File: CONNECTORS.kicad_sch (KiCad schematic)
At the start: 0 parts

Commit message: added micro and 3 sensors and connectors with USB
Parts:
- added D1: B5819W, Diode_SMD:D_SOD-123, symbol Device:D_Schottky
- added J1: STDC14, Connector_PinHeader_1.27mm:PinHeader_2x07_P1.27mm_Vertical_SMD, symbol Connector:Conn_ST_STDC14
- added J2: Screw_Terminal_01x02, symbol Connector:Screw_Terminal_01x02
- added J3: ARM_SW, Connector_JST:JST_GH_SM02B-GHS-TB_1x02-1MP_P1.25mm_Horizontal, symbol Connector_Generic:Conn_01x02
- added J4: CAMERA, Connector_JST:JST_GH_SM04B-GHS-TB_1x04-1MP_P1.25mm_Horizontal, symbol Connector_Generic:Conn_01x04
- added J5: USB_C, Connector_USB:USB_C_Receptacle_HRO_TYPE-C-31-M-12, symbol Connector:USB_C_Receptacle_USB2.0_16P
- added Q1: AO3401A, Package_TO_SOT_SMD:SOT-23, symbol Transistor_FET:AO3401A
- added R10, R11: 5.1k 1%, Resistor_SMD:R_0603_1608Metric, symbol Device:R
- added R4: 10KΩ 1% 0603, symbol Device:R
- added TP1: BATT_TERM+, symbol Connector:TestPoint
- added TP2: GND, symbol Connector:TestPoint
- added TP3: POST_PFET, symbol Connector:TestPoint
- added U7: USBLC6-2SC6, Package_TO_SOT_SMD:SOT-23-6, symbol Power_Protection:USBLC6-2SC6
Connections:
- new net: D1.2 (A), J5.A4 (VBUS), J5.A9 (VBUS), J5.B4 (VBUS), J5.B9 (VBUS), U7.5 (VBUS)
- new net: J5.A5 (CC1), R10.1
- new net: J5.B5 (CC2), R11.1
- new net: Q1.1 (G), R4.1
- new net +BATT: Q1.2 (S), TP3.1
- new net 3V3: J1.3 (VCC)
- new net 5V0: D1.1 (K), J4.1 (Pin_1)
- new net BATT_RAW: J2.1 (Pin_1), J3.1 (Pin_1), TP1.1
- new net BATT_SW: J3.2 (Pin_2), Q1.3 (D)
- new net CAM_RX: J4.3 (Pin_3)
- new net CAM_TX: J4.2 (Pin_2)
- new net DBG_RX: J1.13 (VCP_RX)
- new net DBG_TX: J1.14 (VCP_TX)
- new net GND: J1.11 (GNDDetect), J1.5 (GND), J1.7 (GND), J2.2 (Pin_2), J4.4 (Pin_4), J5.A1 (GND), J5.A12 (GND), J5.B1 (GND), J5.B12 (GND), J5.SH (SHIELD), R10.2, R11.2, R4.2, TP2.1, U7.2 (GND)
- new net NRST: J1.12 (~{RST})
- new net SWCLK: J1.6 (JCLK/SWCLK)
- new net SWDIO: J1.4 (JTMS/SWDIO)
- new net SWO: J1.8 (JTDO/SWO)
- new net USB_DM: J5.A7 (D-), J5.B7 (D-), U7.3 (I/O2), U7.4 (I/O2)
- new net USB_DP: J5.A6 (D+), J5.B6 (D+), U7.1 (I/O1), U7.6 (I/O1)
- no-connect marks 0 -> 4
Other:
- note added: "BATT_SW"
- note added: "CAM"
- note added: "DEBUGGER"
- note added: "Reverse Polarity"
- note added: "USB-C"

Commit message: added Buzzer, status LEDs
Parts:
- J2: value Screw_Terminal_01x02 -> XT30PW-M; footprint (none) -> Connector_AMASS:AMASS_XT30PW-M_1x02_P2.50mm_Horizontal
- R4: footprint (none) -> Resistor_SMD:R_0603_1608Metric
- TP1, TP2, TP3: footprint (none) -> TestPoint:TestPoint_Pad_D1.5mm
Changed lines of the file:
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@@
 			)
 		)
-		(property "Value" "Screw_Terminal_01x02"
+		(property "Value" "XT30PW-M"
 			(at 20.32 41.9099 0)
 			(hide yes)
@@
 			)
 		)
-		(property "Footprint" ""
+		(property "Footprint" "Connector_AMASS:AMASS_XT30PW-M_1x02_P2.50mm_Horizontal"
 			(at 22.86 39.37 0)
 			(hide yes)
@@
 			)
 		)
-		(property "Footprint" ""
+		(property "Footprint" "TestPoint:TestPoint_Pad_D1.5mm"
 			(at 82.55 35.56 0)
 			(hide yes)
@@
 			)
 		)
-		(property "Footprint" ""
+		(property "Footprint" "TestPoint:TestPoint_Pad_D1.5mm"
 			(at 34.29 35.56 0)
 			(hide yes)
@@
 			)
 		)
-		(property "Footprint" ""
+		(property "Footprint" "TestPoint:TestPoint_Pad_D1.5mm"
 			(at 24.13 41.91 0)
 			(hide yes)
@@
 			)
 		)
-		(property "Footprint" ""
+		(property "Footprint" "Resistor_SMD:R_0603_1608Metric"
 			(at 65.532 52.07 90)
 			(hide yes)

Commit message: Battery protection, camera switch, 64MB flash, ERC clean
- Fuse + TVS on battery input, camera load switch (TPS22917)
- Flash to W25Q512JVFIQ (SOIC-16), hand-solder passive footprints
- Power LED, title blocks, U5 footprint, PWR/NC flags (0 ERC)
- Regenerated schematic PDF
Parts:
- added D5: SMBJ9.0CA, Diode_SMD:D_SMB, symbol Device:D_TVS
- added F1: 3A, Fuse:Fuse_Littelfuse-NANO2-451_453, symbol Device:Fuse
- R10, R11, R4: footprint Resistor_SMD:R_0603_1608Metric -> Resistor_SMD:R_0603_1608Metric_Pad0.98x0.95mm_HandSolder
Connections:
- net 5V0: no longer J4.1 (Pin_1)
- net BATT_RAW: now also D5.2 (A2), F1.2; no longer J2.1 (Pin_1), TP1.1
- net GND: now also D5.1 (A1)
- new net: F1.1, J2.1 (Pin_1), TP1.1
- new net CAM_5V: J4.1 (Pin_1)
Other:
- title: (none) -> Connectors: Battery, Arming, Debug, Camera, USB-C
- moved on the sheet: Q1, R4, TP3

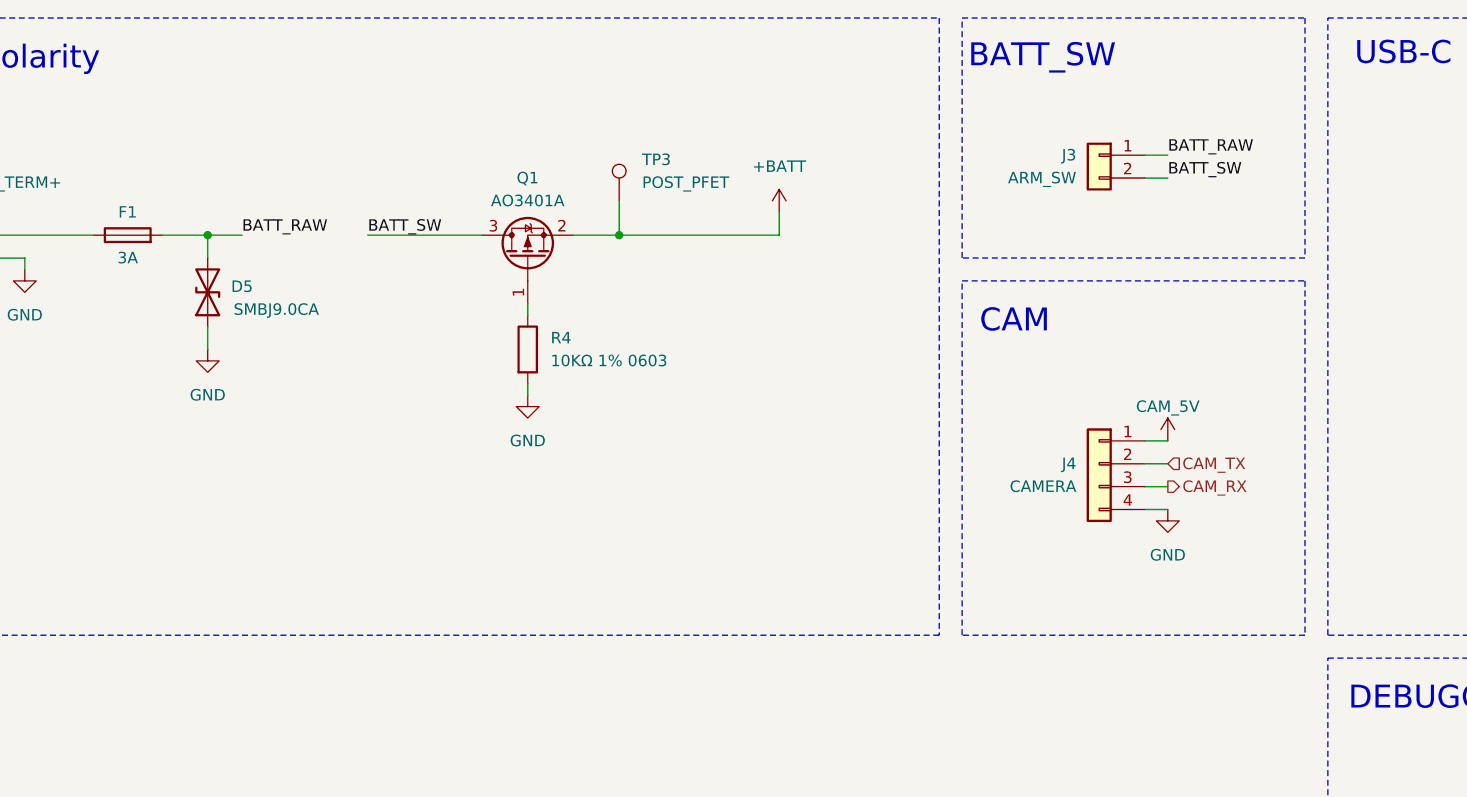
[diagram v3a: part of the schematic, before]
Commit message: updated firmware to fix altitude bug also added mangometer support, updated GUI to have slider for time
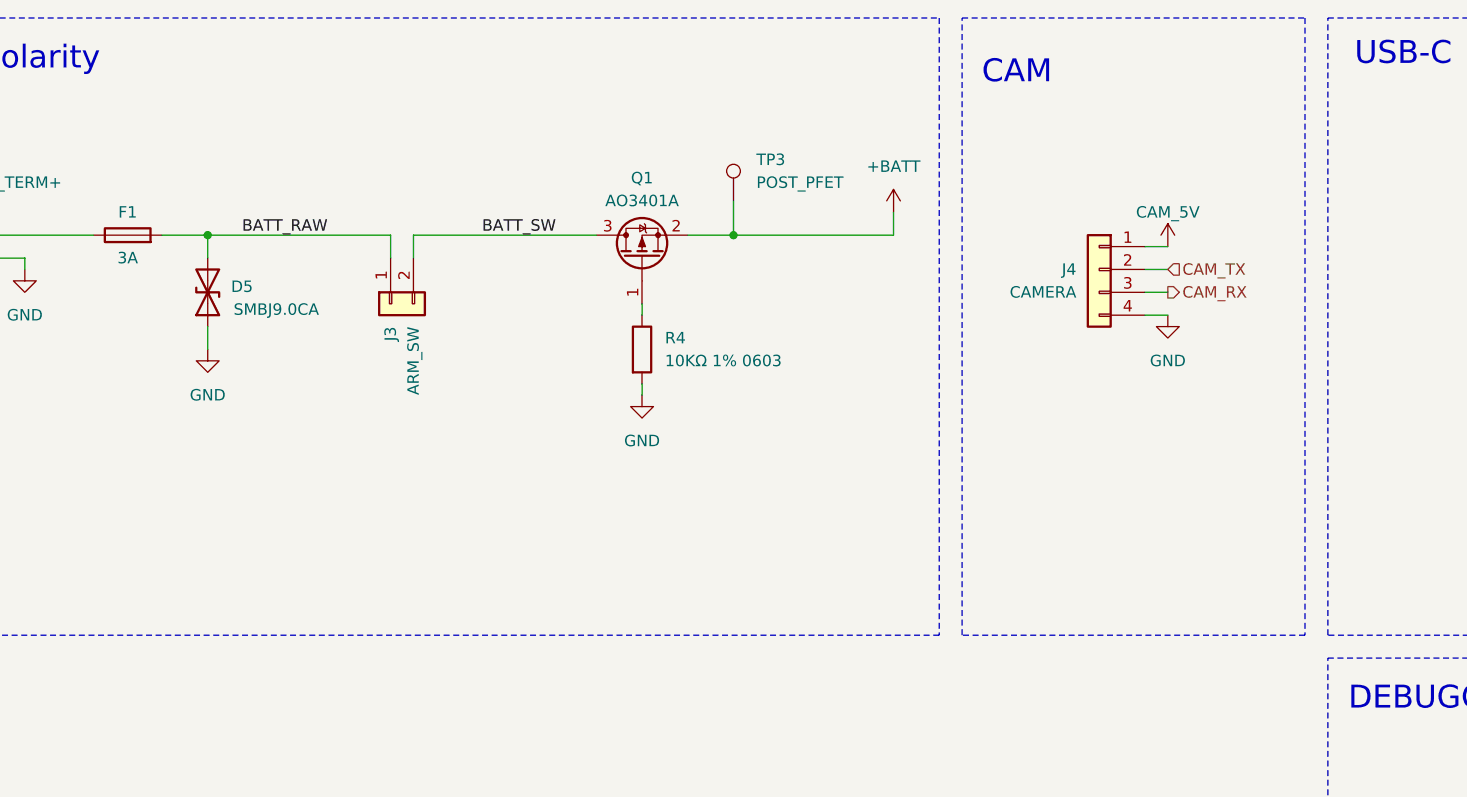
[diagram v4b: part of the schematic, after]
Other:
- note removed: "BATT_SW"
- moved on the sheet: J3, J4, Q1, R4, TP3

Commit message: layed out components, no routing
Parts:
- J2: footprint Connector_AMASS:AMASS_XT30PW-M_1x02_P2.50mm_Horizontal -> Connector_JST:JST_GH_BM02B-GHS-TBT_1x02-1MP_P1.25mm_Vertical
- J3: footprint Connector_JST:JST_GH_SM02B-GHS-TB_1x02-1MP_P1.25mm_Horizontal -> Connector_JST:JST_GH_BM02B-GHS-TBT_1x02-1MP_P1.25mm_Vertical
- J4: footprint Connector_JST:JST_GH_SM04B-GHS-TB_1x04-1MP_P1.25mm_Horizontal -> Connector_JST:JST_GH_BM04B-GHS-TBT_1x04-1MP_P1.25mm_Vertical
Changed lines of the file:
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@@
 			)
 		)
-		(property "Footprint" "Connector_JST:JST_GH_SM04B-GHS-TB_1x04-1MP_P1.25mm_Horizontal"
+		(property "Footprint" "Connector_JST:JST_GH_BM04B-GHS-TBT_1x04-1MP_P1.25mm_Vertical"
 			(at 158.75 43.18 0)
 			(hide yes)
@@
 			)
 		)
-		(property "Footprint" "Connector_AMASS:AMASS_XT30PW-M_1x02_P2.50mm_Horizontal"
+		(property "Footprint" "Connector_JST:JST_GH_BM02B-GHS-TBT_1x02-1MP_P1.25mm_Vertical"
 			(at 22.86 39.37 0)
 			(hide yes)
@@
 			)
 		)
-		(property "Footprint" "Connector_JST:JST_GH_SM02B-GHS-TB_1x02-1MP_P1.25mm_Horizontal"
+		(property "Footprint" "Connector_JST:JST_GH_BM02B-GHS-TBT_1x02-1MP_P1.25mm_Vertical"
 			(at 80.01 46.99 0)
 			(hide yes)
